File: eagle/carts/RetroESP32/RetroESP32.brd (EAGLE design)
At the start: 50.2 x 61 mm, 13 parts, among them J5 503182-1852_503182-1852, Q4 mmbt2222, Q5 mmbt2222, U1 ESP32-WROVER_ESP32-WROVER

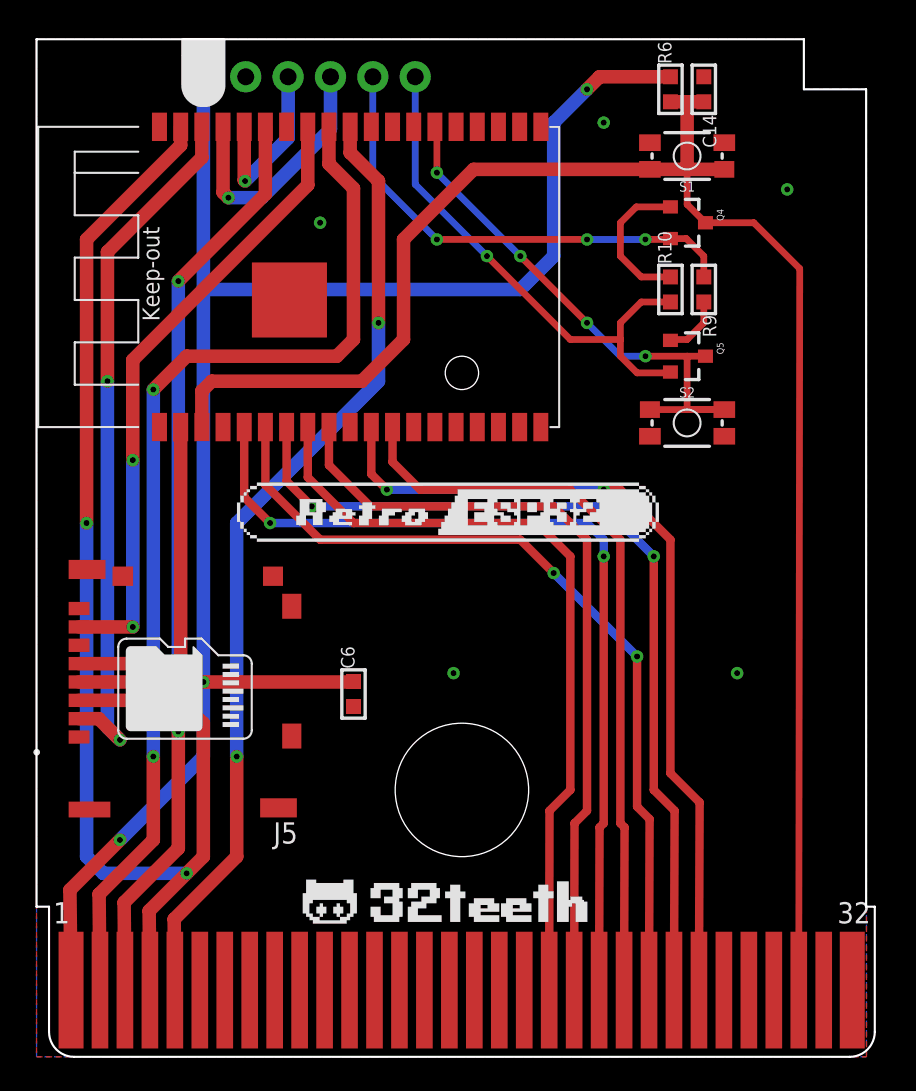
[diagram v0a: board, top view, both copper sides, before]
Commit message: feat: update USB and VCC lines on ATMega
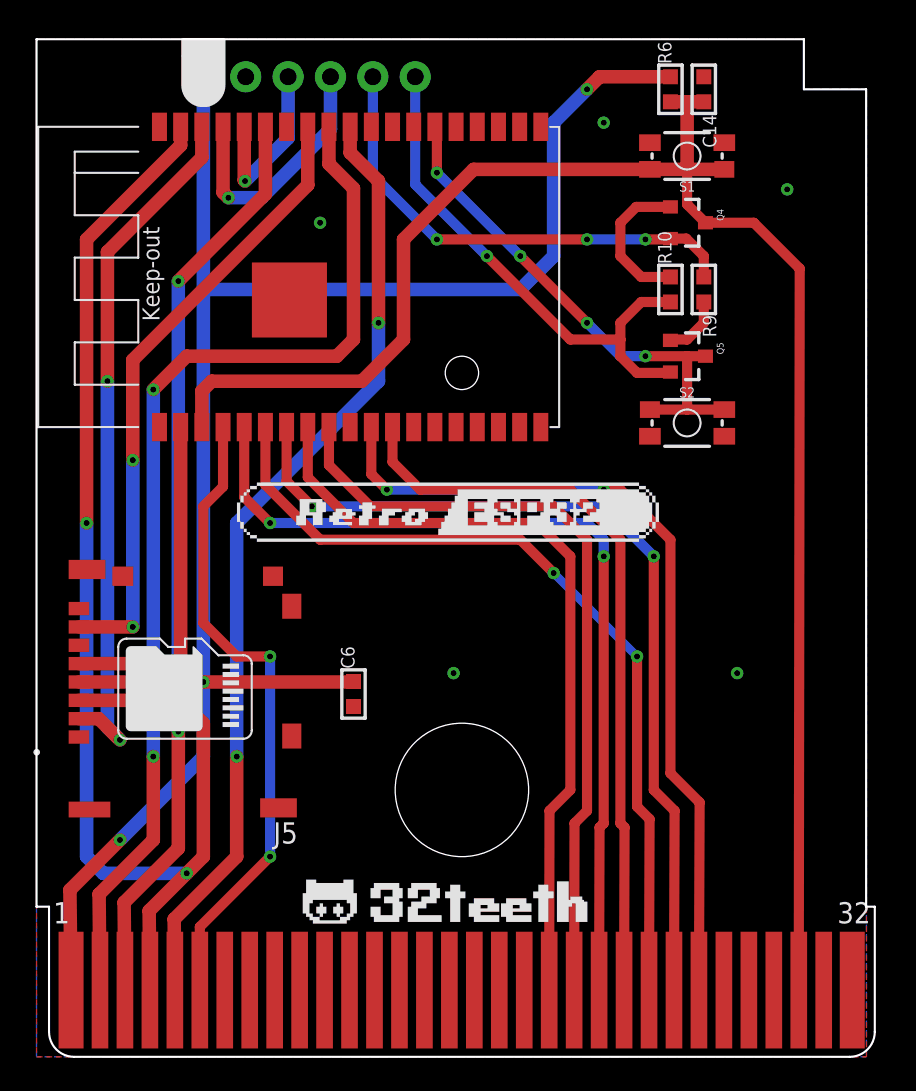
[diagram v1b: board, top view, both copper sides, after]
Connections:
- net GPIO36: now also U$2.6
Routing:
- net GPIO36: track 0.00 -> 38.8 mm, vias 0 -> 2
